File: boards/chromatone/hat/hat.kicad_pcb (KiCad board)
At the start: 2 copper layers, 50 x 50 mm, 0 parts

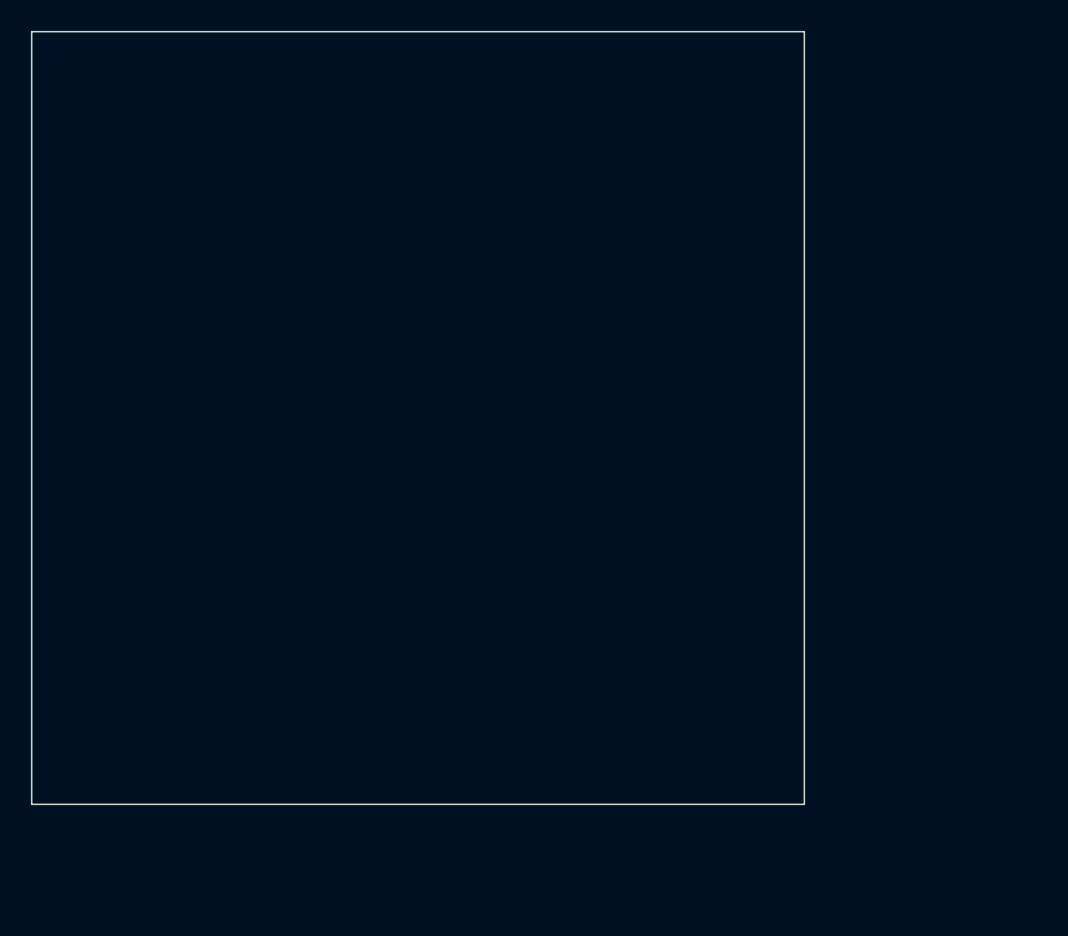
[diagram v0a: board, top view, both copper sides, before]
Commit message: chromatone/hat: PCB step 1, outline + holes + back-side header (DRC clean without parity)
generate/pcb.py places the HAT mechanics: 65 x 56.5 mm with 3 mm corners, holes at
58 x 49, the 2x20 socket on the back with pin 1 at (8.37, 4.77), 5V pins 2+4 joined
on the front, 3V3 pins 1+17 joined on the back under the socket, GND pads 6/9/14
(whose pour slivers that link cuts off) solid-connected and stitched by a front stub
and via, and the Pi-domain pour as two overlapping rectangles that leave the LED
island (x > 44.5, y > 30) empty. generate/drc.sh is the regenerate-and-report loop.

pcbgen fixes found on the way: flipped footprints now mirror pad/text `at` too (the
header's pin row ran the wrong way), gr_arc midpoints are written with 6 decimals
(4 leave a gap KiCad reports as an open outline), and Board() drops gr_arc/circle/poly
from the template so a generator that reads its own output does not accumulate arcs.

Co-Authored-By: Claude Fable 5.1 <noreply@anthropic.com>
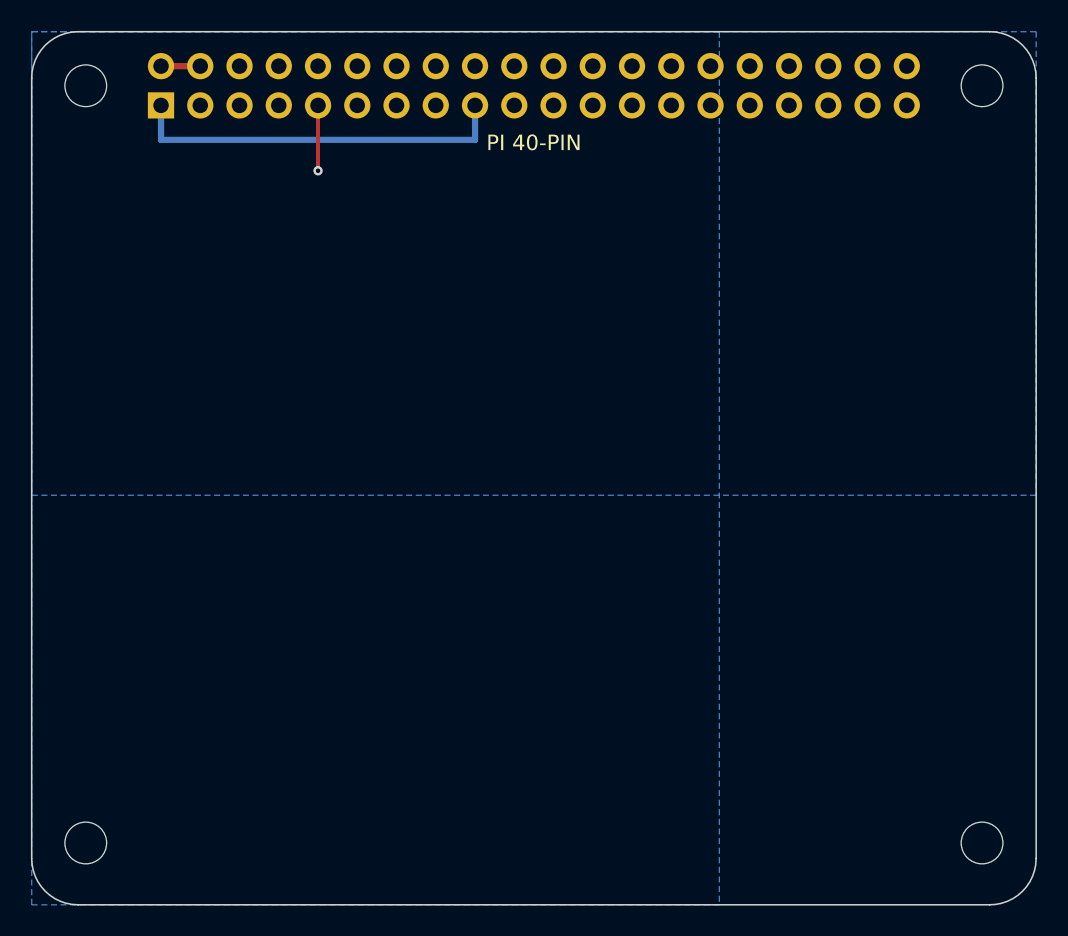
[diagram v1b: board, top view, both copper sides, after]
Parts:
- added H1: M2.5, MountingHole:MountingHole_2.7mm_M2.5, F.Cu at (53.5, 53.5)
- added H2: M2.5, MountingHole:MountingHole_2.7mm_M2.5, F.Cu at (111.5, 53.5)
- added H3: M2.5, MountingHole:MountingHole_2.7mm_M2.5, F.Cu at (53.5, 102.5)
- added H4: M2.5, MountingHole:MountingHole_2.7mm_M2.5, F.Cu at (111.5, 102.5)
- added J1: Pi 40-pin, Connector_PinSocket_2.54mm:PinSocket_2x20_P2.54mm_Vertical, B.Cu at (58.4, 54.8)
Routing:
- net +3V3: track 0.00 -> 24.8 mm
- net GND: track 0.00 -> 4.23 mm, vias 0 -> 1
- net +5V: track 0.00 -> 2.54 mm
- added copper zone on B.Cu, net GND
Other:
- board size 50 x 50 mm -> 65 x 56.5 mm
- board text added: "PI 40-PIN"
- board text added: "chromatone/hat rev A"

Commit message: chromatone/hat: PCB step 2, DAC block rotated onto the right half (internally DRC clean)
The chromatone/dac rev A placement and routing is reused through T(x, y) =
(31 + y, 56.5 - x): jack on the bottom edge at x = 53, PCM5102A at (48, 19.5), the
33 R I2S resistors in a row under the header with pad 1 facing it, LDO at (37, 23.5).
Pad points are tagged (Pt) so the segment helper transforms only old-coordinate
literals. The LED island moves to the bottom left (x < 21.5, y > 31.5). Remaining
opens are the five header connections (5V, BCK, LRCK, DIN, XSMT) and the isolator.

Co-Authored-By: Claude Fable 5.1 <noreply@anthropic.com>
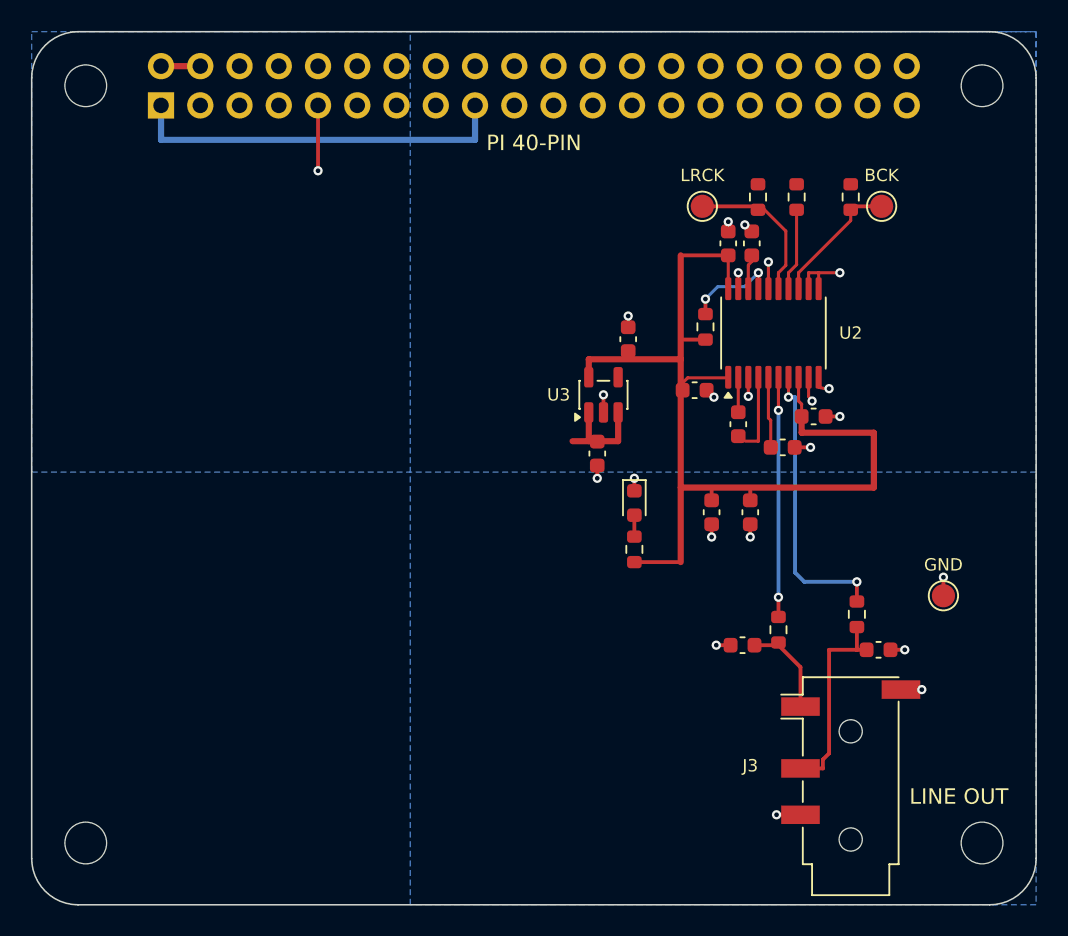
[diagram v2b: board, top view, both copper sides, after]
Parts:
- added C10: 2.2u, Capacitor_SMD:C_0603_1608Metric, F.Cu at (98.6, 76.9)
- added C11: 2.2u, Capacitor_SMD:C_0603_1608Metric, F.Cu at (96.6, 63.7)
- added C12: 2.2n, Capacitor_SMD:C_0603_1608Metric, F.Cu at (96.0, 89.7)
- added C13: 2.2n, Capacitor_SMD:C_0603_1608Metric, F.Cu at (104.8, 90.0)
- added C14: 100n, Capacitor_SMD:C_0603_1608Metric, F.Cu at (100.6, 74.9)
- added C15: 100n, Capacitor_SMD:C_0603_1608Metric, F.Cu at (95.1, 63.7)
- added C16: 100n, Capacitor_SMD:C_0603_1608Metric, F.Cu at (92.9, 73.2)
- added C5: 10u, Capacitor_SMD:C_0603_1608Metric, F.Cu at (86.6, 77.3)
- added C6: 10u, Capacitor_SMD:C_0603_1608Metric, F.Cu at (88.6, 69.9)
- added C7: 10u, Capacitor_SMD:C_0603_1608Metric, F.Cu at (94.0, 81.1)
- added C8: 10u, Capacitor_SMD:C_0603_1608Metric, F.Cu at (96.5, 81.1)
- added C9: 2.2u, Capacitor_SMD:C_0603_1608Metric, F.Cu at (95.7, 75.4)
- added D3: GREEN, LED_SMD:LED_0603_1608Metric, F.Cu at (89.0, 80.5)
- added J3: Line out, Connector_Audio:Jack_3.5mm_PJ320D_Horizontal, F.Cu at (103.0, 97.5)
- added R10: 10k, Resistor_SMD:R_0603_1608Metric, F.Cu at (93.6, 69.1)
- added R11: 1k, Resistor_SMD:R_0603_1608Metric, F.Cu at (89.0, 83.5)
- added R5: 33, Resistor_SMD:R_0603_1608Metric, F.Cu at (97.0, 60.7)
- added R6: 33, Resistor_SMD:R_0603_1608Metric, F.Cu at (99.5, 60.7)
- added R7: 33, Resistor_SMD:R_0603_1608Metric, F.Cu at (103.0, 60.7)
- added R8: 470, Resistor_SMD:R_0603_1608Metric, F.Cu at (98.3, 88.7)
- added R9: 470, Resistor_SMD:R_0603_1608Metric, F.Cu at (103.4, 87.7)
- added TP7: LRCK, TestPoint:TestPoint_Pad_D1.5mm, F.Cu at (93.4, 61.3)
- added TP8: BCK, TestPoint:TestPoint_Pad_D1.5mm, F.Cu at (105.0, 61.3)
- added TP9: GND, TestPoint:TestPoint_Pad_D1.5mm, F.Cu at (109.0, 86.5)
- added U2: PCM5102A, Package_SO:TSSOP-20_4.4x6.5mm_P0.65mm, F.Cu at (98.0, 69.5)
- added U3: ME6211C33, Package_TO_SOT_SMD:SOT-23-5, F.Cu at (87.0, 73.5)
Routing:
- net +3V3_DAC: track 0.00 -> 66.0 mm
- net GND: track 4.23 -> 29.9 mm, vias 1 -> 23
- net Net-(U2-OUTR): track 0.00 -> 18.6 mm, vias 0 -> 2
- net Net-(U2-OUTL): track 0.00 -> 15.5 mm, vias 0 -> 2
- net Net-(C13-Pad1): track 0.00 -> 13.2 mm
- net Net-(U2-LRCK): track 0.00 -> 9.90 mm
- net Net-(U2-BCK): track 0.00 -> 8.51 mm
- net +5V: track 2.54 -> 9.24 mm
- net Net-(C12-Pad1): track 0.00 -> 6.29 mm
- net /XSMT: track 0.00 -> 6.14 mm, vias 0 -> 2
- net Net-(U2-DIN): track 0.00 -> 5.33 mm
- net Net-(U2-CAPM): track 0.00 -> 4.96 mm
- net Net-(U2-VNEG): track 0.00 -> 4.12 mm
- net Net-(U2-CAPP): track 0.00 -> 2.26 mm
- net Net-(U2-LDOO): track 0.00 -> 2.26 mm
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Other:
- board text added: "LINE OUT"

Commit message: chromatone/hat: PCB step 3, header escapes for the DAC (DRC clean without parity)
5V leaves pad 4 on the back, down the west side and east along y = 26.5 to the LDO
feed; BCK leaves pad 12 on the back along y = 6.3 under the socket to a via by R7;
LRCK and DIN come down the front on parallel 45 deg runs to their resistors; XSMT
hops under the DAC rail to the existing XSMT via. The 3V3 pin 1/17 link moves to the
front. Pad 25 (GND), whose pour sliver the BCK run isolates, gets a stub, via and
solid connection.

Co-Authored-By: Claude Fable 5.1 <noreply@anthropic.com>
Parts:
- moved TP7 0.90 mm to (92.5, 61.3)
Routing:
- net /BCK: track 0.00 -> 47.6 mm, vias 0 -> 1
- net +5V: track 9.24 -> 56.1 mm, vias 0 -> 1
- net /XSMT: track 6.14 -> 18.8 mm, vias 2 -> 3
- net /DIN: track 0.00 -> 11.7 mm
- net /LRCK: track 0.00 -> 7.33 mm
- net +3V3: track 24.8 -> 23.6 mm
- net Net-(U2-LRCK): track 9.90 -> 10.8 mm

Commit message: chromatone/hat: PCB step 4, isolator block + 3V3/SPI feeds (DRC clean without parity)
chromatone/isolator rev A rotated 180 deg into the bottom left: J2 on the left edge,
U1 on a vertical 3 mm barrier at x = 23, LED island x < 21.5, y > 31.5 with its own
GND_LED pour, hole H3 inside it. MOSI (pin 19) and SCLK (pin 23) come down the middle
as columns at x = 32 / 34; 3V3 (pin 17) hops under them on the back, runs down x = 35.5
with a jog past the LDO, and feeds C2/U1 from below as in the original. R3/D1 moved
below C2, TP1/TP2/TP5 moved clear of the feeds.

Co-Authored-By: Claude Fable 5.1 <noreply@anthropic.com>
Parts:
- added C1: 100n, Capacitor_SMD:C_0603_1608Metric, F.Cu at (77.5, 92.7)
- added C2: 10u, Capacitor_SMD:C_0603_1608Metric, F.Cu at (79.0, 96.1)
- added C3: 100n, Capacitor_SMD:C_0603_1608Metric, F.Cu at (68.5, 92.7)
- added C4: 10u, Capacitor_SMD:C_0603_1608Metric, F.Cu at (67.0, 96.1)
- added D1: GREEN, LED_SMD:LED_0603_1608Metric, F.Cu at (86.5, 101.5)
- added D2: BLUE, LED_SMD:LED_0603_1608Metric, F.Cu at (67.5, 82.5)
- added J2: Strip, Connector_JST:JST_XH_B4B-XH-A_1x04_P2.50mm_Vertical, F.Cu at (54.5, 95.5)
- added R1: 47, Resistor_SMD:R_0603_1608Metric, F.Cu at (65.0, 90.6)
- added R2: 47, Resistor_SMD:R_0603_1608Metric, F.Cu at (65.0, 88.2)
- added R3: 1k, Resistor_SMD:R_0603_1608Metric, F.Cu at (82.5, 101.5)
- added R4: 1k, Resistor_SMD:R_0603_1608Metric, F.Cu at (63.5, 82.5)
- added TP1: SCLK, TestPoint:TestPoint_Pad_D1.5mm, F.Cu at (83.5, 96.0)
- added TP2: MOSI, TestPoint:TestPoint_Pad_D1.5mm, F.Cu at (82.0, 84.0)
- added TP3: CLK, TestPoint:TestPoint_Pad_D1.5mm, F.Cu at (62.0, 95.0)
- added TP4: DATA, TestPoint:TestPoint_Pad_D1.5mm, F.Cu at (61.0, 84.5)
- added TP5: GND_A, TestPoint:TestPoint_Pad_D1.5mm, F.Cu at (87.5, 87.0)
- added TP6: GND_B, TestPoint:TestPoint_Pad_D1.5mm, F.Cu at (64.5, 86.0)
- added U1: ISO7720D, Package_SO:SOIC-8_3.9x4.9mm_P1.27mm, F.Cu at (73.0, 90.0)
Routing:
- net +3V3: track 23.6 -> 94.0 mm, vias 0 -> 2
- net /SCLK: track 0.00 -> 51.9 mm
- net +5V_LED: track 0.00 -> 46.3 mm
- net /MOSI: track 0.00 -> 40.3 mm
- net Net-(J2-Pin_2): track 0.00 -> 15.0 mm
- net Net-(J2-Pin_3): track 0.00 -> 14.3 mm
- net GND_LED: track 0.00 -> 7.46 mm, vias 0 -> 5
- net GND: track 29.9 -> 37.1 mm, vias 23 -> 28
- net Net-(U1-OUTB): track 0.00 -> 5.18 mm
- net Net-(U1-OUTA): track 0.00 -> 4.70 mm
- net Net-(D2-A): track 0.00 -> 2.39 mm
- net Net-(D1-A): track 0.00 -> 2.39 mm
- added copper zone on B.Cu, net GND_LED
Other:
- board text added: "5V"
- board text added: "CI"
- board text added: "DI"
- board text added: "GND"
- board text added: "ISOLATED"
- board text added: "LED 5V"

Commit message: chromatone/hat: PCB step 5, ID EEPROM block; board ERC/DRC clean with parity
DNP 24LC32 with its pull-ups, WP jumper and 100 nF in the left-centre on a 3V3 rail
tapped off the pin 1/17 link; ID_SD/ID_SC drop from pins 27/28 to vias and run west
on the back under the SPI columns. READMEs describe the built layout.

pcbgen: keep library attr tokens other than the netlist-driven bom/pos/dnp flags
(allow_soldermask_bridges on solder jumpers was being dropped, which produced a
mask-bridge warning and a library-mismatch warning).

Co-Authored-By: Claude Fable 5.1 <noreply@anthropic.com>
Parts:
- added C17: 100n, Capacitor_SMD:C_0603_1608Metric, F.Cu at (63.2, 63.0)
- added JP1: WP, Jumper:SolderJumper-2_P1.3mm_Open_RoundedPad1.0x1.5mm, F.Cu at (73.8, 63.6)
- added R12: 3.9k, Resistor_SMD:R_0603_1608Metric, F.Cu at (75.5, 68.9)
- added R13: 3.9k, Resistor_SMD:R_0603_1608Metric, F.Cu at (78.5, 67.6)
- added R14: 10k, Resistor_SMD:R_0603_1608Metric, F.Cu at (75.5, 66.4)
- added U4: 24LC32, Package_SO:SOIC-8_3.9x4.9mm_P1.27mm, F.Cu at (68.0, 67.0)
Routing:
- net /ID_SC: track 0.00 -> 41.0 mm, vias 0 -> 2
- net +3V3: track 94.0 -> 133.3 mm
- net /ID_SD: track 0.00 -> 35.3 mm, vias 0 -> 2
- net GND: track 37.1 -> 48.2 mm, vias 28 -> 30
- net Net-(JP1-B): track 0.00 -> 6.96 mm
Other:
- board text added: "ID EEPROM (DNP)"
